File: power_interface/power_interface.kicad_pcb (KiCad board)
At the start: 2 copper layers, 99 x 94 mm, 35 parts, among them J1 Conn_01x02, U1 LM1084-3.3, U2 LM1084-5.0, U3 LM1084-ADJ

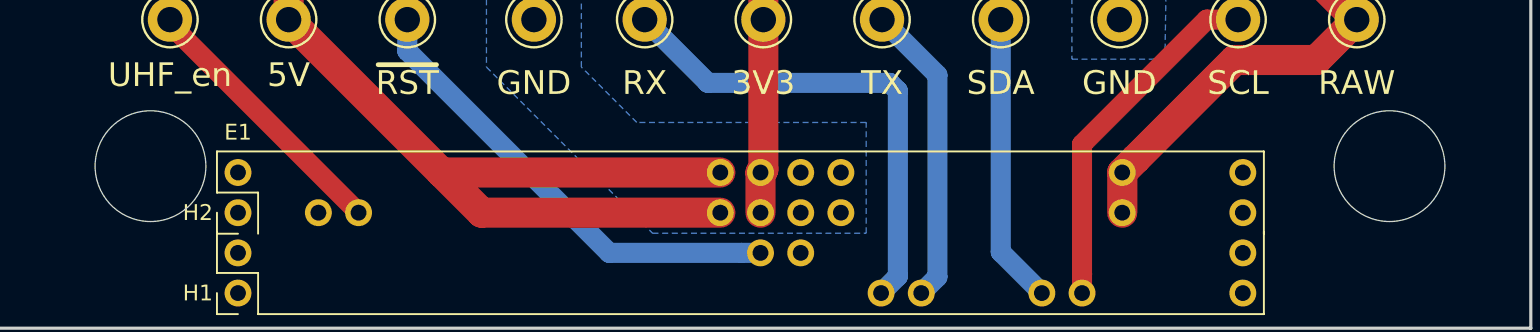
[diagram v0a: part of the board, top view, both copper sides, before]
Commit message: Corrected a misplaced mounting hole. Verified connector layout against the computer board rev_14 layout
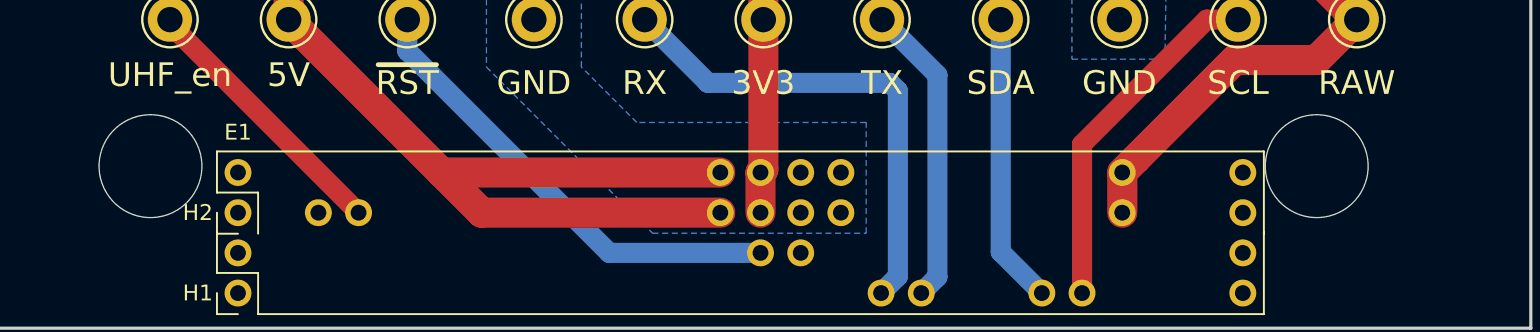
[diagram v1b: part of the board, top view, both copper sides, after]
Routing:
- net (no net): track 0.00 -> 33.4 mm
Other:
- outline, holes or cut-outs redrawn
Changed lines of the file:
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@@
     (thickness 1.6)
     (drawings 25)
-    (tracks 102)
+    (tracks 105)
     (zones 0)
     (modules 35)
@@
     (arrow2b (pts (xy 210.7 137.16) (xy 210.113579 136.033496)))
   )
-  (gr_circle (center 108.77 136.76) (end 112.270014 136.76) (layer Edge.Cuts) (width 0.02))
+  (gr_circle (center 108.77 136.76) (end 112.02 136.76) (layer Edge.Cuts) (width 0.02))
   (dimension 0.4 (width 0.03) (layer F.Fab)
     (gr_text "0.400 mm" (at 100.86 136.96 90) (layer F.Fab)
@@
     (arrow2b (pts (xy 114.3 148.18) (xy 113.173496 148.766421)))
   )
-  (gr_circle (center 187.07 136.76) (end 190.570014 136.76) (layer Edge.Cuts) (width 0.02))
+  (gr_circle (center 182.47 136.76) (end 185.72 136.76) (layer Edge.Cuts) (width 0.02))
   (dimension 0.4 (width 0.03) (layer F.Fab)
     (gr_text "0.400 mm" (at 199.91 136.96 90) (layer F.Fab)
@@
     (arrow2b (pts (xy 198.35 137.16) (xy 197.763579 136.033496)))
   )
-  (dimension 9.27 (width 0.03) (layer F.Fab)
-    (gr_text "9.270 mm" (at 182.435 154.39) (layer F.Fab)
+  (dimension 4.67 (width 0.03) (layer F.Fab)
+    (gr_text "4.670 mm" (at 180.135 154.39) (layer F.Fab)
       (effects (font (size 1.5 1.5) (thickness 0.03)))
     )
-    (feature1 (pts (xy 187.07 136.76) (xy 187.07 153.416421)))
+    (feature1 (pts (xy 182.47 136.76) (xy 182.47 153.416421)))
     (feature2 (pts (xy 177.8 136.76) (xy 177.8 153.416421)))
-    (crossbar (pts (xy 177.8 152.83) (xy 187.07 152.83)))
-    (arrow1a (pts (xy 187.07 152.83) (xy 185.943496 153.416421)))
-    (arrow1b (pts (xy 187.07 152.83) (xy 185.943496 152.243579)))
+    (crossbar (pts (xy 177.8 152.83) (xy 182.47 152.83)))
+    (arrow1a (pts (xy 182.47 152.83) (xy 181.343496 153.416421)))
+    (arrow1b (pts (xy 182.47 152.83) (xy 181.343496 152.243579)))
     (arrow2a (pts (xy 177.8 152.83) (xy 178.926504 153.416421)))
     (arrow2b (pts (xy 177.8 152.83) (xy 178.926504 152.243579)))
@@
     (effects (font (size 1.5 1.5) (thickness 0.3)))
   )
+  (segment (start 84.4 169.4) (end 55.9 169.4) (width 0.3048) (layer In2.Cu) (net 0))
+  (segment (start 78.75 171.65) (end 78.75 174.82) (width 0.3048) (layer In2.Cu) (net 0) (status 20))
+  (segment (start 77.5 170.4) (end 78.75 171.65) (width 0.3048) (layer In2.Cu) (net 0))
   (segment (start 147.08 100.4525) (end 147.08 100.5) (width 2.54) (layer F.Cu) (net 1))
   (segment (start 117.08 100.5) (end 117.08 100.5475) (width 1.27) (layer F.Cu) (net 1))
